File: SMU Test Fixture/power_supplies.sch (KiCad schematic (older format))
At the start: 71 parts, among them J14 Conn_WallSocket_Earth, Q1 TIP36, Q2 TIP35, Q3 TIP36, Q4 BD139, Q5 BD140, Q6 BD139, T1 Transformer_1P_1S, T2 Transformer_1P_2S, U10 LT3045xMSE-1, U11 LT3094xMSE, U9 MIC29510-5.0WT

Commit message: Add Zenner to keep xfrmr output below LT3045 abs max on low load, remove cap multiplier
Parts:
- removed C32, C33, C35, C36: 470u, Capacitor_THT:CP_Radial_D12.5mm_P5.00mm, symbol Device:CP_Small
- removed C38, C39: 1m, Capacitor_SMD:CP_Elec_16x22, symbol Device:CP_Small
- removed C46, C47: 5.6m, symbol Device:CP_Small
- removed D45, D46, D49, D50, D51, D52: D, symbol Device:D
- removed Q1: TIP36, Package_TO_SOT_THT:TO-247-3_Vertical, symbol Device:Q_PNP_BCE
- removed Q2: TIP35, Package_TO_SOT_THT:TO-247-3_Vertical, symbol Device:Q_NPN_BCE
- removed Q4: BD139, Package_TO_SOT_THT:TO-126-3_Vertical, symbol Transistor_BJT:BD139
- removed Q5: BD140, Package_TO_SOT_THT:TO-126-3_Vertical, symbol Transistor_BJT:BD140
- removed R31, R32, R34, R35: 220R, symbol Device:R_US
- removed R37, R38: 12k, symbol Device:R_US
- added C? (x2): 4.7u, symbol Device:C_Small
- C? (x2): value C_Small -> 10u
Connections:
- wire segments 299 -> 231
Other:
- moved on the sheet: C26, C27, C29, C30, C43, C44, C?, D39, D40, D43, D44, D?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

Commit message: Change txfrmrs to VPP series, change 10V txfrmr to 12V to improve regulation
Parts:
- added D?: Vz=18V, symbol Device:D_Zener
- T1: value Transformer_1P_1S -> VPP12-4400; footprint eaton:XFMR_F-371P -> XFMR_VPP12-4400; symbol multiplexer:F-371P -> multiplexer:VPP12-4400; MANUFACTURER (none) -> Triad Magnetics; PN VPP10-3000 -> VPP12-4400; STANDARD (none) -> Manufacturer Recommendations
- T2: value Transformer_1P_2S -> VPP36-820; footprint eaton:TRANSFORMER_FS28-1300-C2 -> XFMR_VPP36-820; symbol multiplexer:FS28-1300-C2 -> multiplexer:VPP36-820; MANUFACTURER (none) -> TRIAD; PN FS28-1300-C2 -> VPP36-820; STANDARD (none) -> IPC-7251
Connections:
- net GND: now also T2.12, D?.2 (A); no longer T2.6, T2.7
- net at C27.2, C30.2, C?.2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: now also D?.2 (A)
- net at C26.1, C29.1, C?.1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: now also D?.1 (K)
- net at F2.2, T1.7: now also T1.10; no longer T1.5
- net at J14.2 (AC_N), T2.4: now also T1.3, T1.6, T2.1; no longer T1.2, T1.4
- net at T1.1, TH1.1: now also T1.4, T2.3, T2.6; no longer T1.3, T2.1
- net at D41.2 (A), D42.1 (K): now also T1.12, T1.9; no longer T1.6, T1.8
- net at C40.1, D53.2 (A), Q3.2 (C)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: now also D?.1 (K)
- new net: F3.2, T2.10, T2.7
- new net: F4.2, T2.9
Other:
- moved on the sheet: C26, C27, C28, C29, C30, C31, C34, C37, C40, C43, C44, C45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

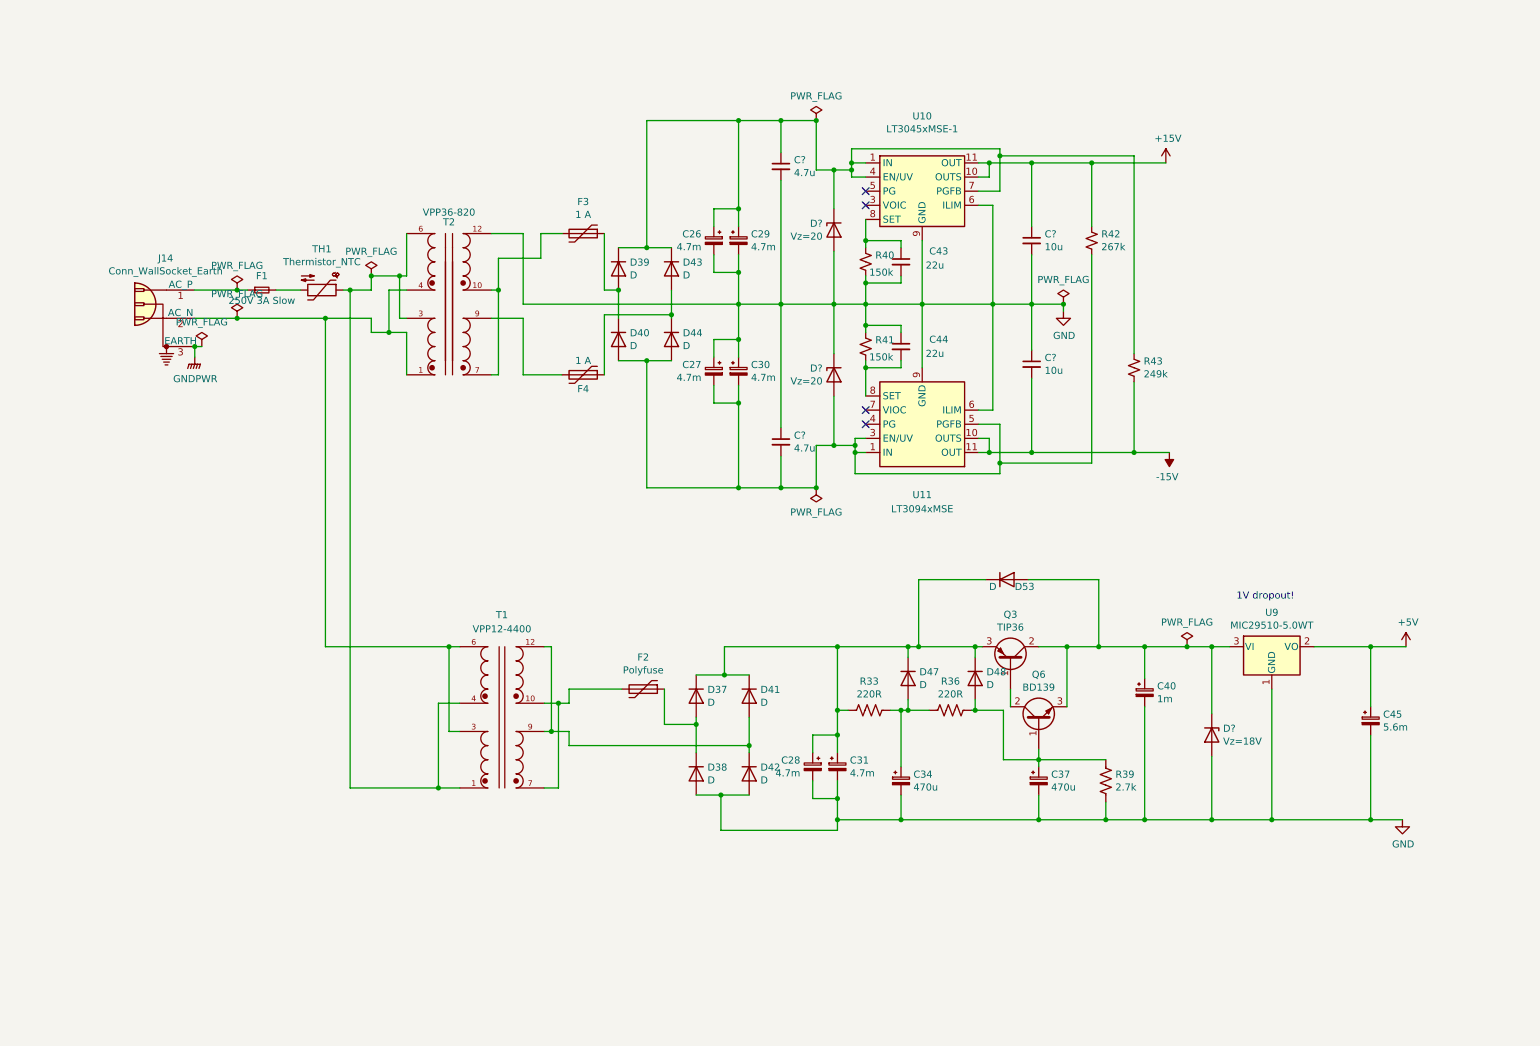
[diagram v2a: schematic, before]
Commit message: Remove mysterious output resistors from 3094 app note.
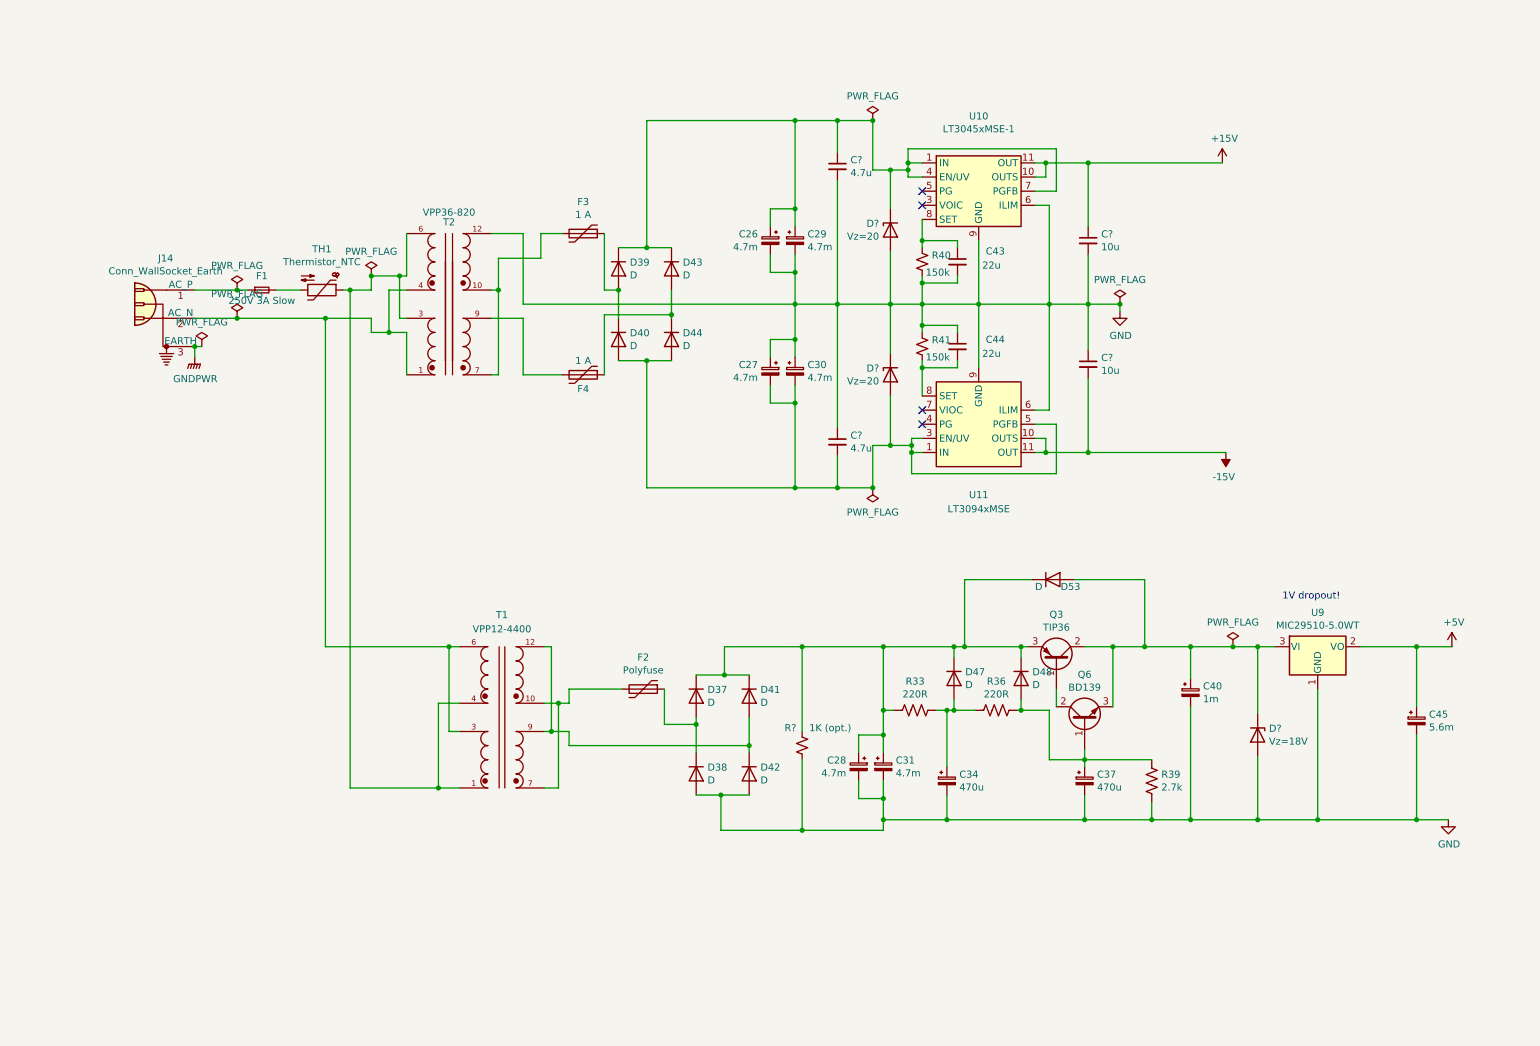
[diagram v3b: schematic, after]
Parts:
- removed R42: 267k, symbol Device:R_Small_US
- removed R43: 249k, symbol Device:R_Small_US
- added R?: 1K (opt.), symbol Device:R_Small_US
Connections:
- net GND: now also R?.2
- net at C28.1, C31.1, D37.1 (K)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: now also R?.1
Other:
- moved on the sheet: C26, C27, C28, C29, C30, C31, C34, C37, C40, C43, C44, C45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

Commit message: Add SCR pre-reg for +15V rail
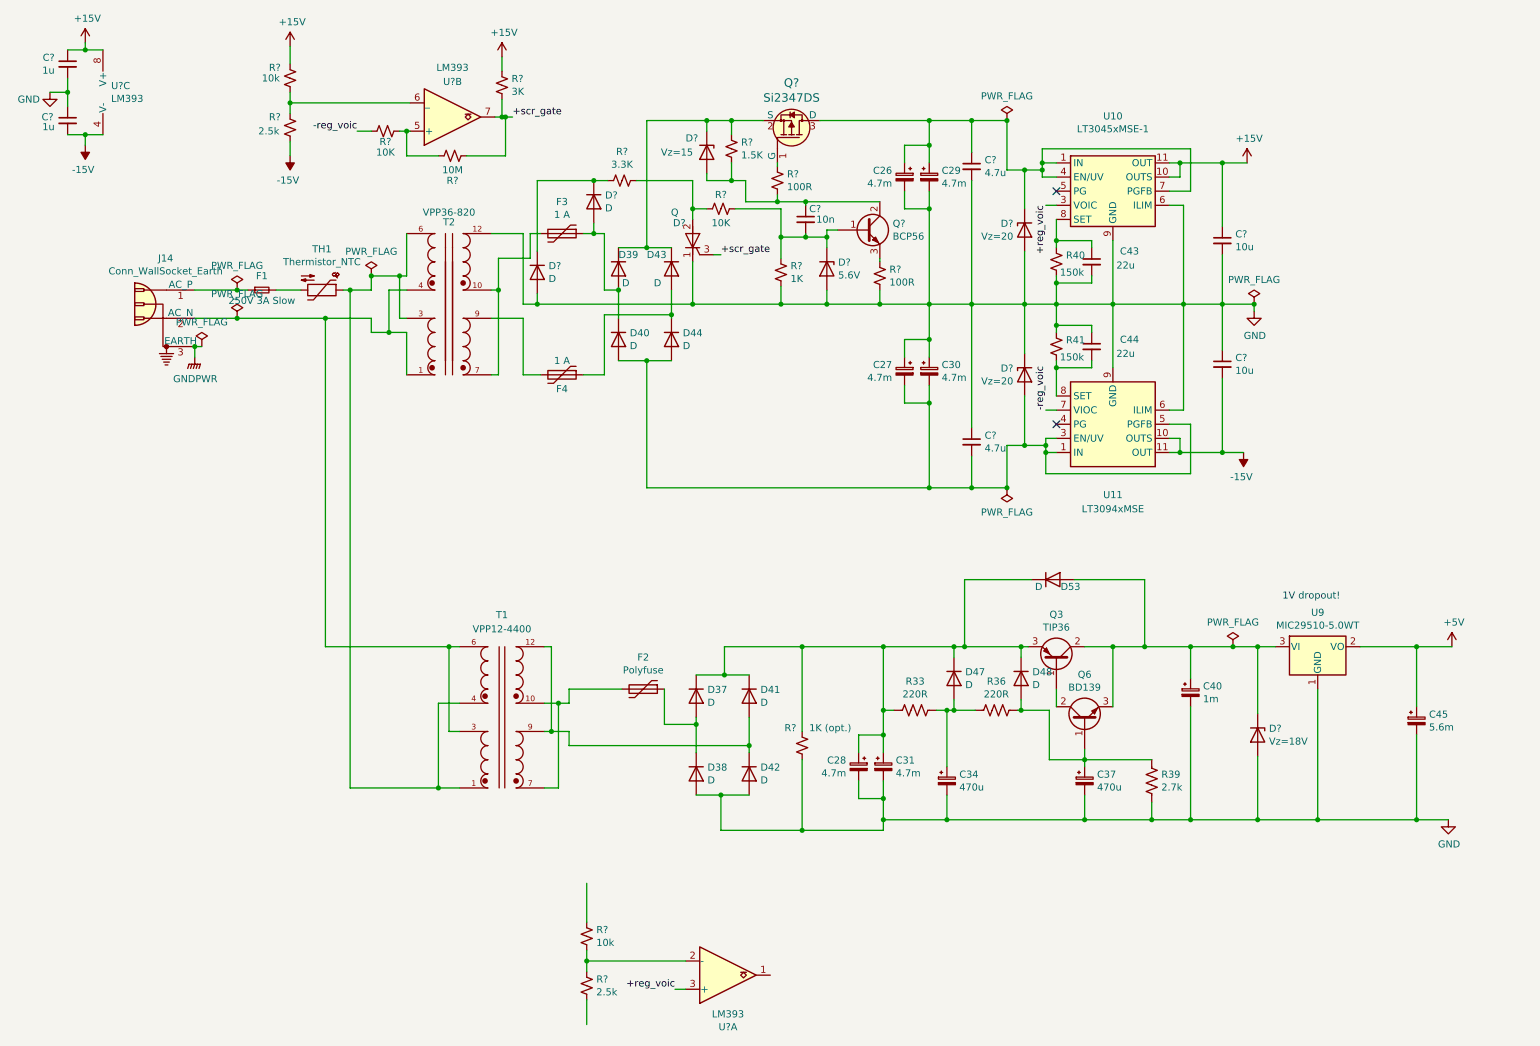
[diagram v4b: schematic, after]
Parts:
- added C? (x2): 1u, symbol Device:C_Small
- added C?: 10n, symbol Device:C_Small
- added D?: Vz=15, symbol Device:D_Zener
- added D? (x2): D, symbol Device:D
- added D?: Q, symbol Device:Q_SCR_KAG
- added D?: 5.6V, symbol Device:D_Zener
- added Q?: Si2347DS, digikey-footprints:SOT-23-3, symbol dk_Transistors-FETs-MOSFETs-Single:DMG2305UX-13
- added Q?: BCP56, Package_TO_SOT_SMD:SOT-223-3_TabPin2, symbol Transistor_BJT:BCP56
- added R? (x2): 10k, symbol Device:R_Small_US
- added R? (x2): 2.5k, symbol Device:R_Small_US
- added R?: 1.5K, symbol Device:R_Small_US
- added R? (x2): 100R, symbol Device:R_Small_US
- added R?: 3.3K, symbol Device:R_Small_US
- added R? (x2): 10K, symbol Device:R_Small_US
- added R?: 1K, symbol Device:R_Small_US
- added R?: 3K, symbol Device:R_Small_US
- added R?: 10M, symbol Device:R_Small_US
- added U? (x3): LM393, symbol Comparator:LM393
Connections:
- net +15V: now also C?.1, R?.1, R?.1, U?.8 (V+)
- net -15V: now also C?.2, R?.2, U?.4 (V-)
- net GND: now also C?.1, C?.2, D?.1 (K), D?.2 (A), D?.2 (A), R?.2, R?.2
- net -reg_voic: now reaches U11.7 (VIOC)
- net -reg_voic: now also R?.2
- net at C26.1, C29.1, C?.1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: now also Q?.3 (D); no longer D39.1 (K), D43.1 (K)
- net +reg_voic: now reaches U10.3 (VOIC)
- net +reg_voic: now also U?.3 (+)
- net at D39.2 (A), D40.1 (K), F3.1: now also D?.2 (A)
- new net: D39.1 (K), D43.1 (K), D?.1 (K), Q?.2 (S), R?.1
- new net: R?.1, R?.2, U?.2 (-)
- new net: R?.1, R?.2, U?.5 (+)
- new net: R?.1, R?.2, U?.6 (_)
- new net: Q?.1 (G), R?.1
- new net: C?.1, D?.2 (A), Q?.2 (C), Q?.4 (C), R?.2, R?.2
- new net: D?.1 (K), D?.1 (K), R?.2
- new net: D?.2 (A), R?.1, R?.2
- new net: C?.2, D?.1 (K), Q?.1 (B), R?.1, R?.1
- new net: Q?.3 (E), R?.1
- new net +scr_gate: D?.3 (G), R?.1, R?.2, U?.7
- no-connect marks 4 -> 2
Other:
- moved on the sheet: C26, C27, C29, C30, C43, C44, C?, D?, F3, F4, R40, R41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

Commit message: Add SCR pre-reg for -15V rail
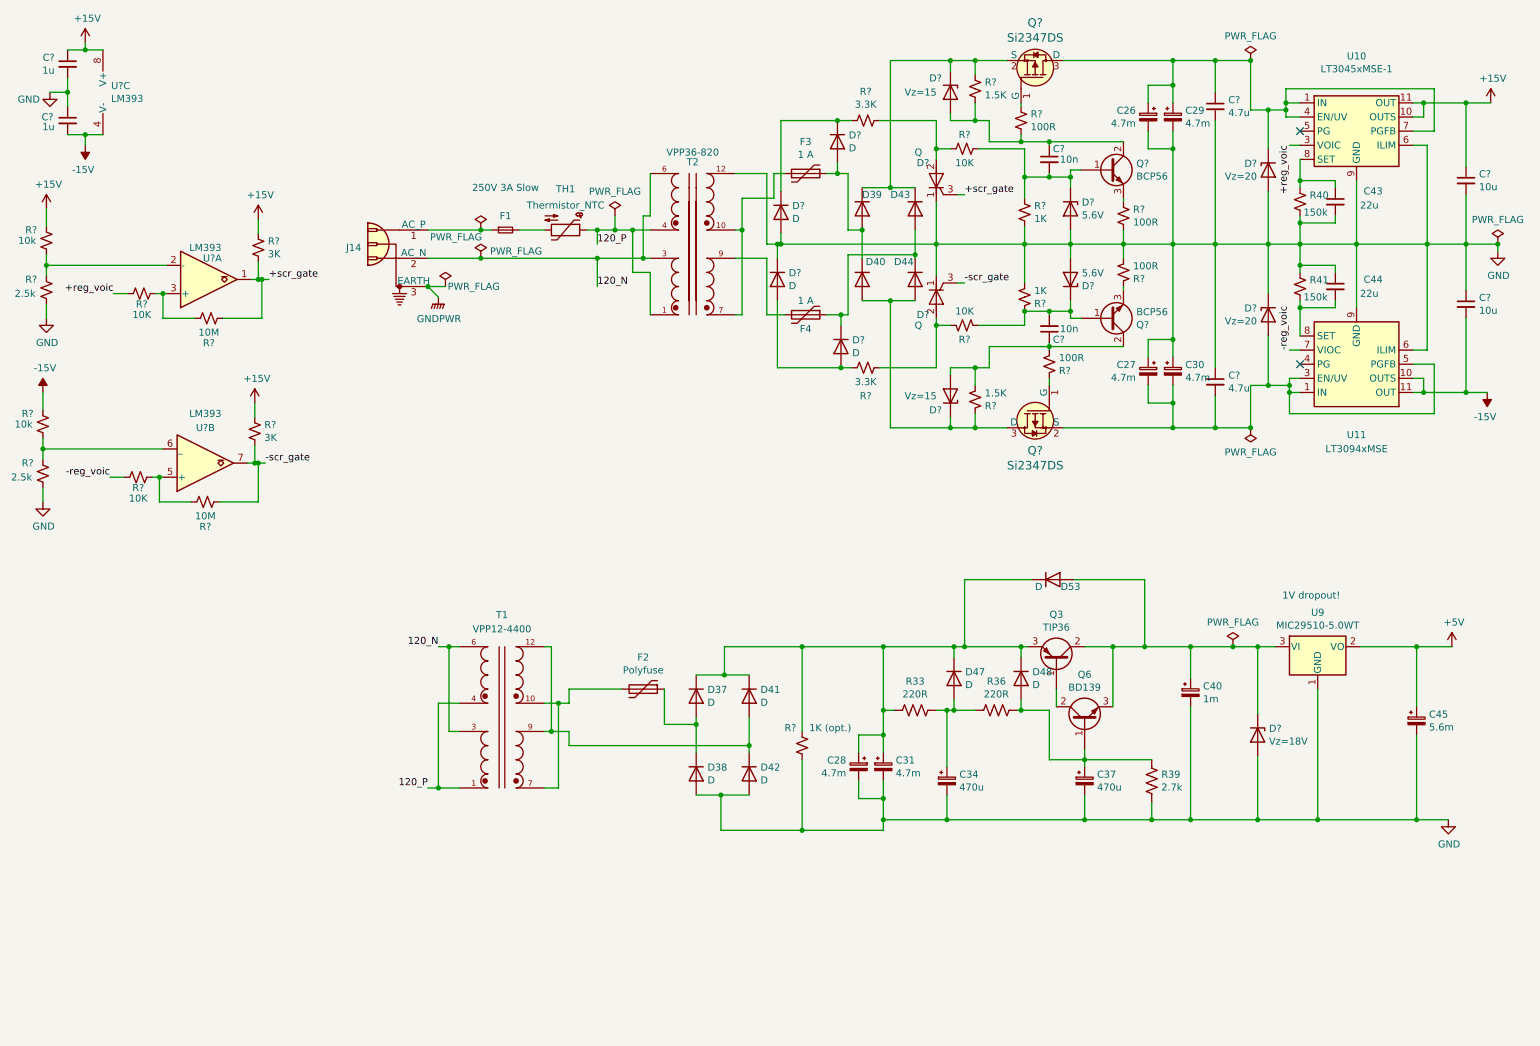
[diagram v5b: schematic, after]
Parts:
- removed R?: 10k, symbol Device:R_Small_US
- removed R?: 2.5k, symbol Device:R_Small_US
- added C?: 10n, symbol Device:C_Small
- added D? (x2): D, symbol Device:D
- added D?: Q, symbol Device:Q_SCR_KAG
- added D?: Vz=15, symbol Device:D_Zener
- added D?: 5.6V, symbol Device:D_Zener
- added Q?: Si2347DS, digikey-footprints:SOT-23-3, symbol dk_Transistors-FETs-MOSFETs-Single:DMG2305UX-13
- added Q?: BCP56, Package_TO_SOT_SMD:SOT-223-3_TabPin2, symbol Transistor_BJT:BCP56
- added R?: 10k, symbol Device:R_Small_US
- added R?: 2.5k, symbol Device:R_Small_US
- added R?: 3K, symbol Device:R_Small_US
- added R? (x2): 10K, symbol Device:R_Small_US
- added R?: 10M, symbol Device:R_Small_US
- added R?: 3.3K, symbol Device:R_Small_US
- added R?: 1K, symbol Device:R_Small_US
- added R?: 1.5K, symbol Device:R_Small_US
- added R? (x2): 100R, symbol Device:R_Small_US
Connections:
- net +15V: now also R?.1, R?.1; no longer R?.1
- net +reg_voic: now also R?.2; no longer U?.3 (+)
- net +scr_gate: now also U?.1, R?.1, R?.2; no longer R?.1, R?.2, U?.7
- net -15V: now also R?.1; no longer R?.2
- net GND: now also R?.2, D?.1 (K), D?.1 (K), D?.2 (A), R?.2, R?.2, R?.2
- net at C27.2, C30.2, C?.2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: now also Q?.2 (S); no longer D40.2 (A), D44.2 (A)
- net at D43.2 (A), D44.1 (K), F4.1: now also D?.1 (K)
- net 120_N: now reaches J14.2 (AC_N), T1.3, T1.6
- net 120_N: now also T2.3, T2.6; no longer T2.1, T2.4
- net 120_P: now reaches T1.1, T1.4, TH1.1
- net 120_P: now also T2.1, T2.4; no longer T2.3, T2.6
- net at U?.2 (-): now also R?.1, R?.2
- new net: D40.2 (A), D44.2 (A), D?.1 (K), Q?.3 (D), R?.1
- new net: R?.1, R?.2, U?.3 (+)
- new net: D?.2 (A), D?.2 (A), R?.2
- new net: D?.2 (A), R?.1, R?.2
- new net: C?.2, D?.1 (K), Q?.1 (B), R?.1, R?.1
- new net: Q?.1 (G), R?.1
- new net: C?.1, D?.2 (A), Q?.2 (C), Q?.4 (C), R?.2, R?.2
- new net: Q?.3 (E), R?.1
- new net -scr_gate: D?.3 (G), R?.1, R?.2, U?.7
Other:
- moved on the sheet: C26, C27, C29, C30, C43, C44, C?, D39, D40, D43, D44, D?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

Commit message: Add SCR pre-reg for 5V rail
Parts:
- removed R?: 1K (opt.), symbol Device:R_Small_US
- added C?: 1n, symbol Device:C_Small
- added D?: Vz=15, symbol Device:D_Zener
- added D? (x2): D, symbol Device:D
- added D?: Q, symbol Device:Q_SCR_KAG
- added D?: 5.6V, symbol Device:D_Zener
- added Q?: Si2347DS, digikey-footprints:SOT-23-3, symbol dk_Transistors-FETs-MOSFETs-Single:DMG2305UX-13
- added Q?: BCP56, Package_TO_SOT_SMD:SOT-223-3_TabPin2, symbol Transistor_BJT:BCP56
- added Q?: BC857, Package_TO_SOT_SMD:SOT-23, symbol Transistor_BJT:BC857
- added R? (x2): 100R, symbol Device:R_Small_US
- added R?: 1.5K, symbol Device:R_Small_US
- added R?: 3.3K, symbol Device:R_Small_US
- added R?: 10K, symbol Device:R_Small_US
- added R?: 1K, symbol Device:R_Small_US
- added R?: 4.7K, symbol Device:R_Small_US
- added R?: 4.7K, symbol Device:R_US
- added R?: 39K, symbol Device:R_Small_US
- added R?: 390K, symbol Device:R_Small_US
- added RV?: 100K, symbol Device:R_POT_US
- C? (x2): value 10n -> 1n
- Q3: value TIP36 -> NJVMJB42CT4G; footprint (none) -> Package_TO_SOT_SMD:TO-263-3_TabPin4; symbol Device:Q_PNP_BCE -> Device:Q_PNP_BCEC
- Q6: value BD139 -> BCP56; footprint (none) -> Package_TO_SOT_SMD:SOT-223-3_TabPin2; symbol Device:Q_NPN_BCE -> Transistor_BJT:BCP56
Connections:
- net +5V: now also R?.2
- net GND: now also D?.2 (A), D?.1 (K), D?.2 (A), R?.2, R?.2, R?.2; no longer D?.1 (K)
- net at D37.2 (A), D38.1 (K), F2.1: now also D?.2 (A)
- net at D43.2 (A), D44.1 (K), F4.1: now also D?.2 (A); no longer D?.1 (K)
- net at D41.2 (A), D42.1 (K), T1.12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: now also D?.2 (A)
- net at C28.1, C31.1, D47.1 (K)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: now also Q?.3 (D); no longer D37.1 (K), D41.1 (K)
- net at C40.1, D53.2 (A), D?.1 (K)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: now also Q3.4 (C), Q?.2 (E), R?.2; no longer Q3.2 (C)
- net at Q3.1 (B), Q6.2 (C): now also Q6.4 (C)
- new net: D37.1 (K), D41.1 (K), D?.1 (K), Q?.2 (S), R?.1
- new net: D?.1 (K), D?.1 (K), R?.2 (x2)
- new net: Q?.1 (G), R?.1
- new net: C?.1, D?.2 (A), Q?.2 (C), Q?.4 (C), R?.2, R?.2
- new net: D?.2 (A), R?.1, R?.2
- new net: C?.2, D?.1 (K), Q?.1 (B), R?.1, R?.1
- new net: Q?.3 (E), R?.1
- new net: Q?.1 (B), R?.1, RV?.1
- new net: Q?.3 (C), R?.1
- new net: R?.1, RV?.2, RV?.3
- new net 5V_scr_gate: D?.3 (G), R?.1, R?.2
- no-connect marks 2 -> 3
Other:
- note removed: "1V dropout!"
- moved on the sheet: D37, D38, D41, D42, F2, T1
